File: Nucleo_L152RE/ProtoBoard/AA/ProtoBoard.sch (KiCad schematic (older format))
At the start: 114 parts, among them CON1 USB-MICRO-B, J1 EXT1, J2 EXT2, J3 EXTPower, P1 Power, P10 OW2_A, P11 GND1, P12 I2C1_B, P13 I2C2_B, P14 SW_1_6, P15 WS1, P16 WS2, P17 MS2, P18 WS3, P19 WS4, P2 VinPower, P20 GND2, P21 Hole, P22 MS3, P23 OW3_A, P24 OW4_A, P25 MS4, P26 Hole, P27 Hole, P28 RGB1, P29 Ant, P3 USART2, P30 Hole, P4 SWD Header, P5 USART1, P6 MS1, P7 I2C1_A, P8 I2C2_A, P9 OW1_A, Q1 SI2323DS, SW1 MomentarySwitch, U2 Nucleo-L152RE-CN7, U3 Nucleo-L152RE-CN10, U5 MT3329_GPS, U6 S25FL127S, U7 RFM69HW

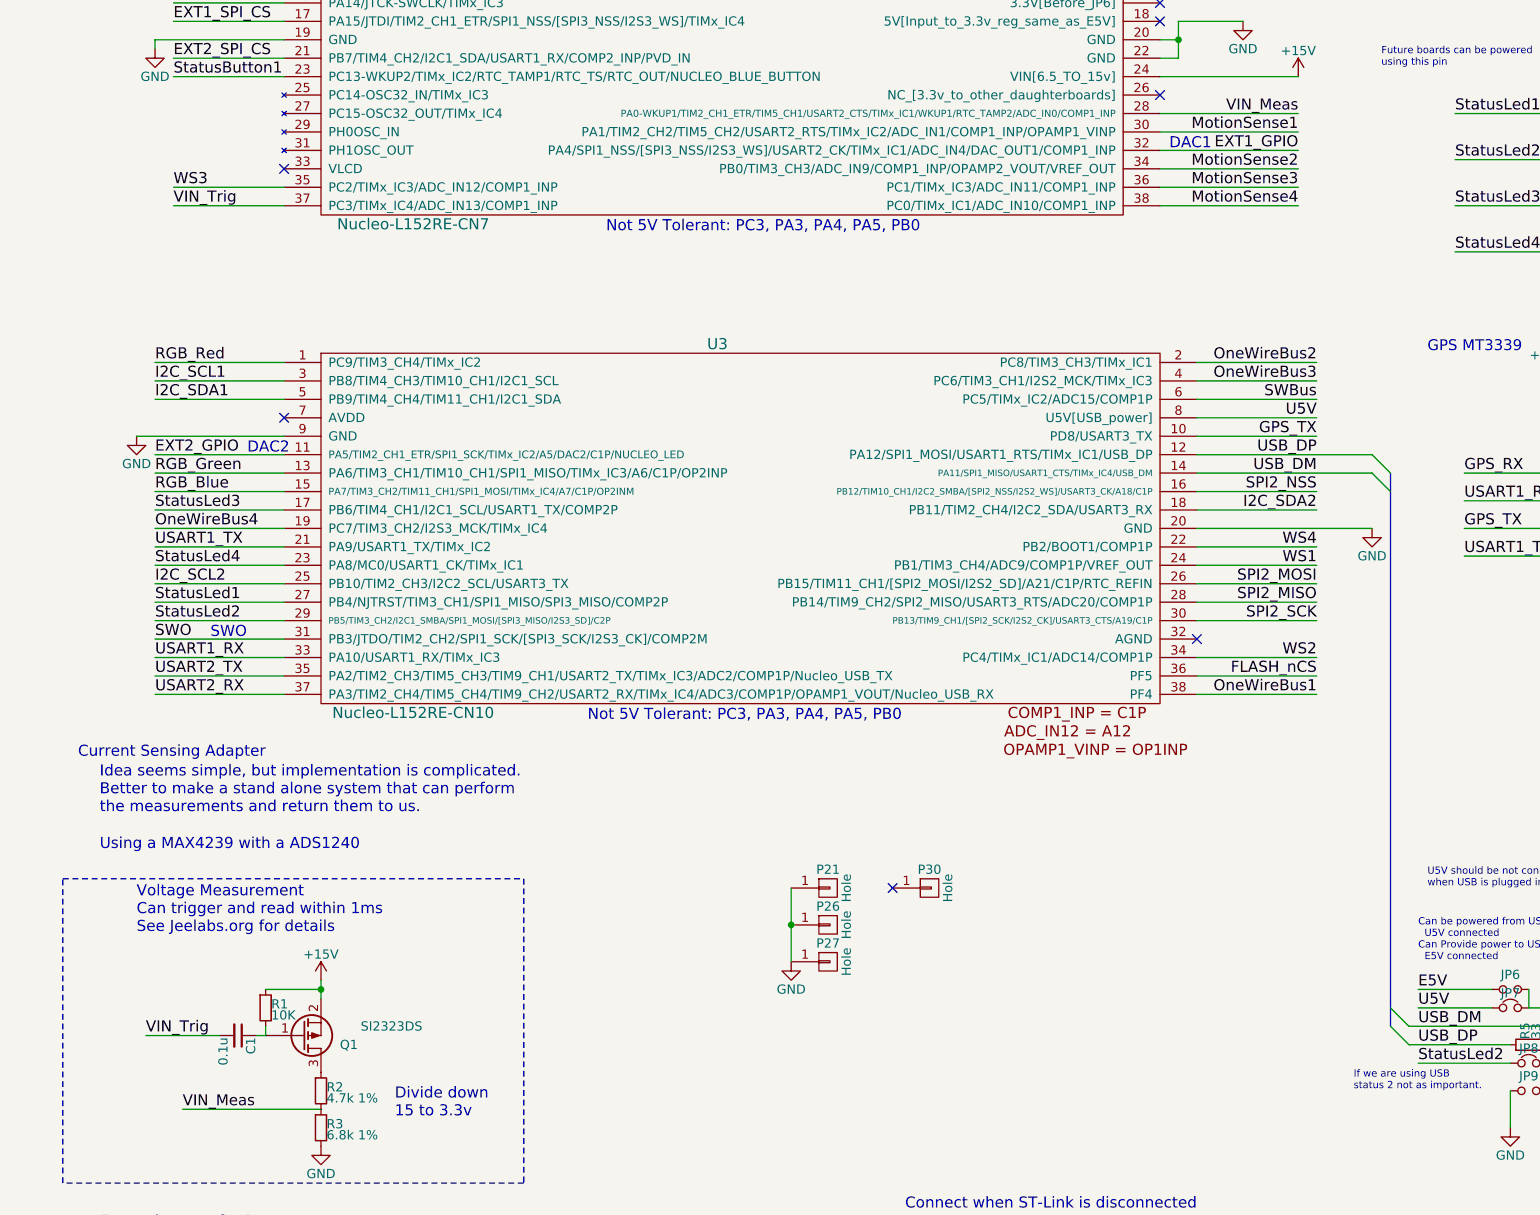
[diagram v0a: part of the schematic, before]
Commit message: Fixed Flash and Pmos footprints.  Added symbol part for schematic.
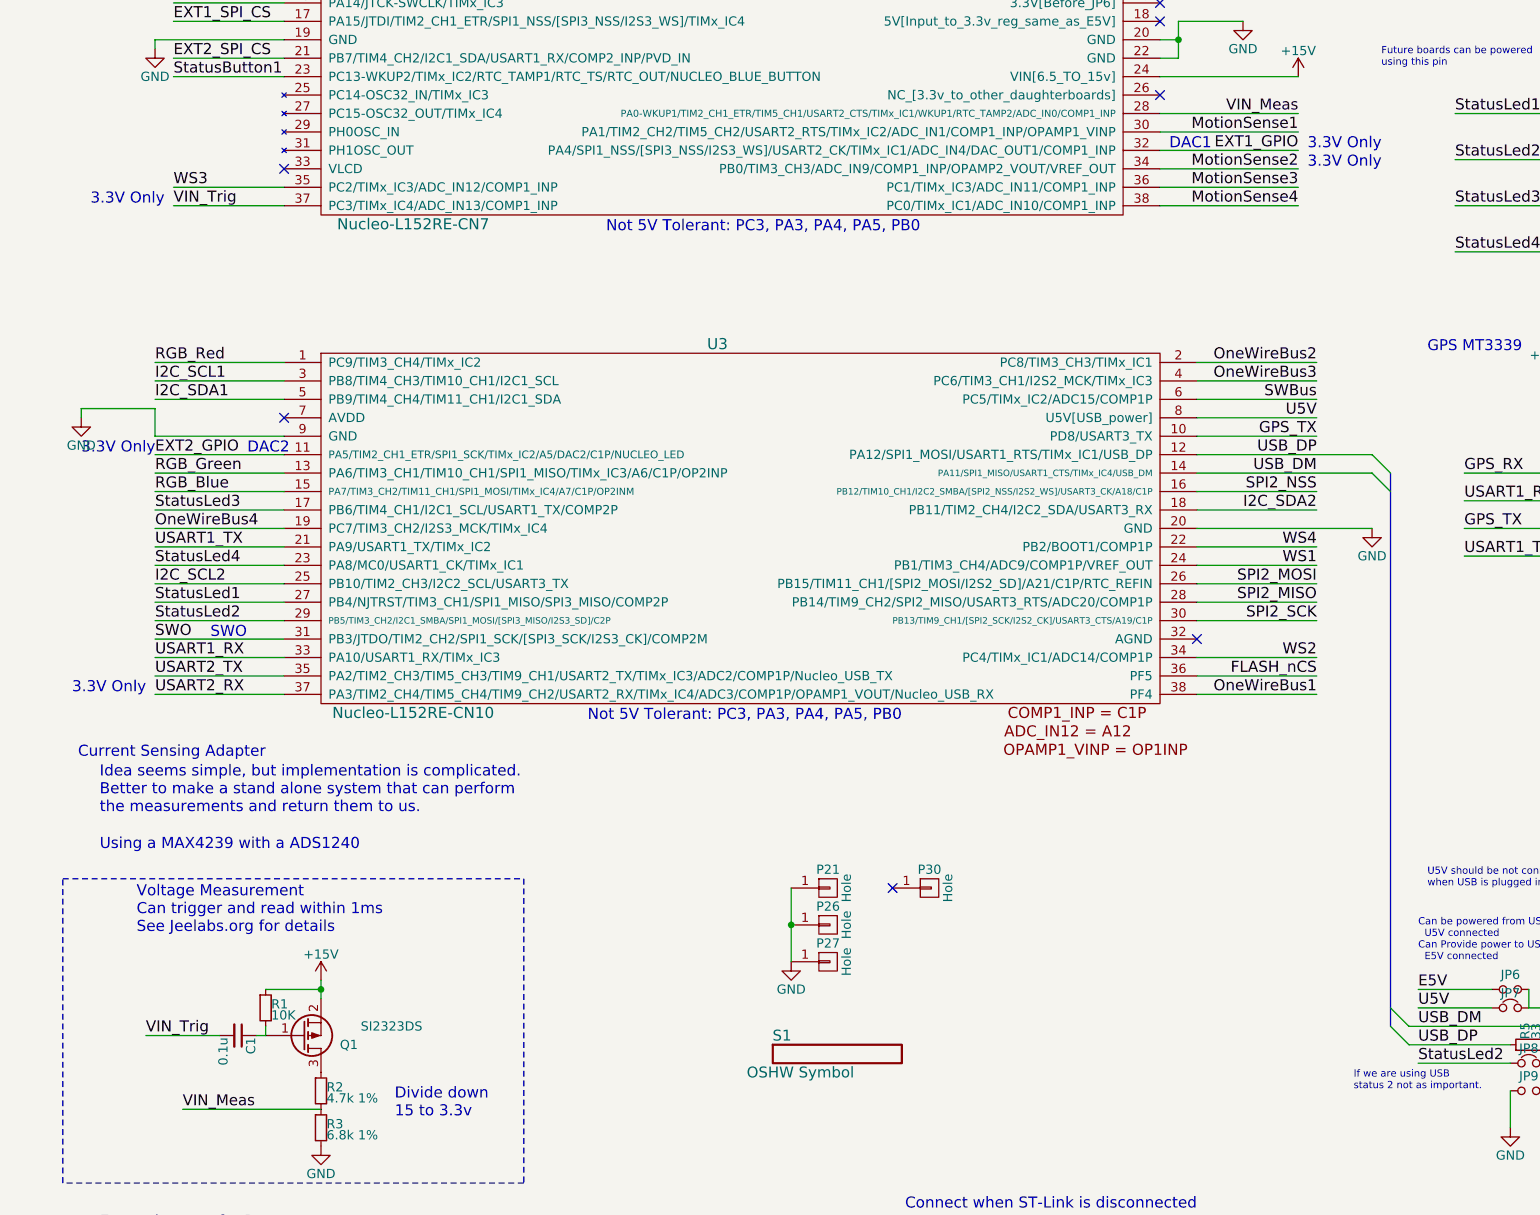
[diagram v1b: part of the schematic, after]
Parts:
- added S1: OSHW Symbol, Symbols:Symbol_OSHW-Logo_SilkScreen, symbol Symbol
- Q1: footprint SMD_Packages:SOT-323 -> nucleo:TO-236
- U6: footprint SMD_Packages:SOIC-8-N -> nucleo:SOIC-8-FLASH
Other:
- note added: "3.3V Only"
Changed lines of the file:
@@
 Sheet 1 1
 Title "Expansion Board For STM32 Nucleo-L152RE"
-Date "Wednesday, April 01, 2015"
+Date "Sunday, April 05, 2015"
 Rev "AA"
-Comp "NA"
-Comment1 ""
+Comp "Open Source Hardware"
+Comment1 "Creative Commons - Share Alike"
 Comment2 ""
 Comment3 ""
@@
 F 0 "U6" H 10250 1800 60  0000 C CNN
 F 1 "S25FL127S" H 10100 1300 60  0000 C CNN
-F 2 "SMD_Packages:SOIC-8-N" H 10250 1550 60  0001 C CNN
+F 2 "nucleo:SOIC-8-FLASH" H 10250 1550 60  0001 C CNN
 F 3 "" H 10250 1550 60  0000 C CNN
 	1    10250 1550
@@
 F 0 "Q1" H 2100 7550 50  0000 R CNN
 F 1 "SI2323DS" H 2450 7450 50  0000 R CNN
-F 2 "SMD_Packages:SOT-323" H 2000 7600 29  0001 C CNN
+F 2 "nucleo:TO-236" H 2000 7600 29  0001 C CNN
 F 3 "http://www.vishay.com/docs/72024/72024.pdf" H 1800 7500 60  0001 C CNN
 	1    1800 7500
@@
 F 1 "600 Ohm" V 9880 8610 50  0000 L CNN
 F 2 "Resistors_SMD:R_0603_HandSoldering" H 9850 8650 60  0001 C CNN
-F 3 "http://search.murata.co.jp/Ceramy/image/img/PDF/ENG/L0075S0103LQH3NP_G0.pdf" H 9850 8650 60  0001 C CNN
+F 3 "http://www.digikey.com/product-detail/en/MI0603J601R-10/240-2371-1-ND/806731" H 9850 8650 60  0001 C CNN
 	1    9850 8650
 	0    -1   -1   0
@@
 F 1 "600 Ohm" V 9900 7950 50  0000 L CNN
 F 2 "Resistors_SMD:R_0603_HandSoldering" H 9850 8350 60  0001 C CNN
-F 3 "http://search.murata.co.jp/Ceramy/image/img/PDF/ENG/L0075S0103LQH3NP_G0.pdf" H 9850 8350 60  0001 C CNN
+F 3 "http://www.digikey.com/product-detail/en/MI0603J601R-10/240-2371-1-ND/806731" H 9850 8350 60  0001 C CNN
 	1    9850 8350
 	0    -1   -1   0
@@
 L GND #PWR054
 U 1 1 5525ED88
-P 900 4250
-F 0 "#PWR054" H 900 4000 50  0001 C CNN
-F 1 "GND" H 900 4100 50  0000 C CNN
-F 2 "" H 900 4250 60  0000 C CNN
-F 3 "" H 900 4250 60  0000 C CNN
-	1    900  4250
+P 600 4150
+F 0 "#PWR054" H 600 3900 50  0001 C CNN
+F 1 "GND" H 600 4000 50  0000 C CNN
+F 2 "" H 600 4150 60  0000 C CNN
+F 3 "" H 600 4150 60  0000 C CNN
+	1    600  4150
 	1    0    0    -1
 $EndComp
@@
 	1000 2100 1000 2150
 Wire Wire Line
-	900  4250 1700 4250
-Wire Wire Line
 	6650 4750 7600 4750
 Wire Wire Line
@@
 Wire Wire Line
 	4450 6700 4450 7100
+Text Notes 7250 2800 0    60   ~ 0
+3.3V Only
+Text Notes 600  4350 0    60   ~ 0
+3.3V Only
+Wire Wire Line
+	1700 4250 1000 4250
+Wire Wire Line
+	1000 4250 1000 4100
+Wire Wire Line
+	1000 4100 600  4100
+Wire Wire Line
+	600  4100 600  4150
+Text Notes 550  5650 0    60   ~ 0
+3.3V Only
+Text Notes 7250 2700 0    60   ~ 0
+3.3V Only
+Text Notes 650  3000 0    60   ~ 0
+3.3V Only
+$Comp
+L Symbol S1
+U 1 1 552F8EA1
+P 4650 7600
+F 0 "S1" H 4400 7700 59  0000 C CNN
+F 1 "OSHW Symbol" H 4500 7500 59  0000 C CNN
+F 2 "Symbols:Symbol_OSHW-Logo_SilkScreen" H 4650 7600 59  0001 C CNN
+F 3 "" H 4650 7600 59  0000 C CNN
+	1    4650 7600
+	1    0    0    -1
+$EndComp
 $EndSCHEMATC

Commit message: Adding part details to schematic, creating BOM tools.
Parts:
- CON1: Digikey Part Number (none) -> 609-4053-1-ND; Digikey URL (none) -> http://www.digikey.com/product-detail/en/10104111-0001LF/60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
- D1: Digikey Part Number (none) -> 160-1447-1-ND; Digikey URL (none) -> http://www.digikey.com/product-detail/en/LTST-C191KRKT/160-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
- D2: Digikey Part Number (none) -> 160-1448-1-ND; Digikey URL (none) -> http://www.digikey.com/product-detail/en/LTST-C191KSKT/160-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
- D3: Digikey Part Number (none) -> 160-1446-1-ND; Digikey URL (none) -> http://www.digikey.com/product-detail/en/LTST-C191KGKT/160-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
- D4: Digikey Part Number (none) -> 160-1647-1-ND; Digikey URL (none) -> http://www.digikey.com/product-detail/en/LTST-C191TBKT/160-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
- J1, J2, J3: Digikey Part Number (none) -> RJLSE4238101TTR-ND; Digikey URL (none) -> http://www.digikey.com/product-detail/en/RJLSE4238101T/RJLS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
- L3, L4: Digikey Part Number (none) -> 240-2371-1-ND; Digikey URL (none) -> http://www.digikey.com/product-detail/en/MI0603J601R-10/240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
- SW1: Digikey Part Number (none) -> 450-1650-ND; Digikey URL (none) -> http://www.digikey.com/product-detail/en/1825910-6/450-1650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
- U6: Digikey Part Number (none) -> SI2323DS-T1-E3CT-ND; Digikey URL (none) -> http://www.digikey.com/product-detail/en/SI2323DS-T1-E3/SI2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
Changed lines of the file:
@@
 F 1 "S25FL127S" H 10100 1300 60  0000 C CNN
 F 2 "nucleo:SOIC-8-FLASH" H 10250 1550 60  0001 C CNN
-F 3 "" H 10250 1550 60  0000 C CNN
+F 3 "http://www.digikey.com/product-detail/en/SI2323DS-T1-E3/SI2323DS-T1-E3CT-ND" H 10250 1550 60  0001 C CNN
+F 4 "SI2323DS-T1-E3CT-ND" H 10250 1550 60  0001 C CNN "Digikey Part Number"
+F 5 "http://www.digikey.com/product-detail/en/SI2323DS-T1-E3/SI2323DS-T1-E3CT-ND" H 10250 1550 60  0001 C CNN "Digikey URL"
 	1    10250 1550
 	1    0    0    -1
@@
 F 2 "nucleo:RJ45_SMD" H 9100 9650 60  0001 C CNN
 F 3 "http://www.digikey.com/product-detail/en/RJLSE4238101T/RJLSE4238101TTR-ND/1979556" H 9100 9650 60  0001 C CNN
+F 4 "RJLSE4238101TTR-ND" H 9100 9650 60  0001 C CNN "Digikey Part Number"
+F 5 "http://www.digikey.com/product-detail/en/RJLSE4238101T/RJLSE4238101TTR-ND/1979556" H 9100 9650 60  0001 C CNN "Digikey URL"
 	1    9100 9650
 	0    1    1    0
@@
 F 2 "nucleo:RJ45_SMD" H 11150 9650 60  0001 C CNN
 F 3 "http://www.digikey.com/product-detail/en/RJLSE4238101T/RJLSE4238101TTR-ND/1979556" H 11150 9650 60  0001 C CNN
+F 4 "RJLSE4238101TTR-ND" H 11150 9650 60  0001 C CNN "Digikey Part Number"
+F 5 "http://www.digikey.com/product-detail/en/RJLSE4238101T/RJLSE4238101TTR-ND/1979556" H 11150 9650 60  0001 C CNN "Digikey URL"
 	1    11150 9650
 	0    1    1    0
@@
 F 2 "Resistors_SMD:R_0603_HandSoldering" H 9850 8650 60  0001 C CNN
 F 3 "http://www.digikey.com/product-detail/en/MI0603J601R-10/240-2371-1-ND/806731" H 9850 8650 60  0001 C CNN
+F 4 "240-2371-1-ND" V 9850 8650 60  0001 C CNN "Digikey Part Number"
+F 5 "http://www.digikey.com/product-detail/en/MI0603J601R-10/240-2371-1-ND/" V 9850 8650 60  0001 C CNN "Digikey URL"
 	1    9850 8650
 	0    -1   -1   0
@@
 F 2 "Resistors_SMD:R_0603_HandSoldering" H 9850 8350 60  0001 C CNN
 F 3 "http://www.digikey.com/product-detail/en/MI0603J601R-10/240-2371-1-ND/806731" H 9850 8350 60  0001 C CNN
+F 4 "240-2371-1-ND" V 9850 8350 60  0001 C CNN "Digikey Part Number"
+F 5 "http://www.digikey.com/product-detail/en/MI0603J601R-10/240-2371-1-ND/" V 9850 8350 60  0001 C CNN "Digikey URL"
 	1    9850 8350
 	0    -1   -1   0
@@
 F 1 "Red" H 8800 2420 50  0000 L CNN
 F 2 "nucleo:LED_0603" V 8950 2500 60  0001 C CNN
-F 3 "" V 8950 2500 60  0000 C CNN
+F 3 "http://optoelectronics.liteon.com/upload/download/DS22-2000-223/S_110_LTST-C191KRKT.pdf" V 8950 2500 60  0001 C CNN
+F 4 "160-1447-1-ND" H 8950 2500 60  0001 C CNN "Digikey Part Number"
+F 5 "http://www.digikey.com/product-detail/en/LTST-C191KRKT/160-1447-1-ND/386836" H 8950 2500 60  0001 C CNN "Digikey URL"
 	1    8950 2500
 	1    0    0    -1
@@
 F 1 "Yellow" H 8800 2670 50  0000 L CNN
 F 2 "nucleo:LED_0603" V 8950 2750 60  0001 C CNN
-F 3 "" V 8950 2750 60  0000 C CNN
+F 3 "http://optoelectronics.liteon.com/upload/download/DS22-2000-224/S_110_LTST-C191KSKT.pdf" V 8950 2750 60  0001 C CNN
+F 4 "160-1448-1-ND" H 8950 2750 60  0001 C CNN "Digikey Part Number"
+F 5 "http://www.digikey.com/product-detail/en/LTST-C191KSKT/160-1448-1-ND" H 8950 2750 60  0001 C CNN "Digikey URL"
 	1    8950 2750
 	1    0    0    -1
@@
 F 2 "nucleo:Tact_switch" H 10250 2400 60  0001 C CNN
 F 3 "" H 10250 2400 60  0000 C CNN
+F 4 "450-1650-ND" H 10250 2400 60  0001 C CNN "Digikey Part Number"
+F 5 "http://www.digikey.com/product-detail/en/1825910-6/450-1650-ND" H 10250 2400 60  0001 C CNN "Digikey URL"
 	1    10250 2400
 	1    0    0    -1
@@
 F 2 "nucleo:USB_micro_AB" H 9350 7450 50  0001 C CNN
 F 3 "http://www.digikey.com/product-detail/en/10104111-0001LF/609-4053-1-ND/2350359" H 9350 7450 50  0001 C CNN
+F 4 "609-4053-1-ND" H 9350 7550 60  0001 C CNN "Digikey Part Number"
+F 5 "http://www.digikey.com/product-detail/en/10104111-0001LF/609-4053-1-ND" H 9350 7550 60  0001 C CNN "Digikey URL"
 	1    9350 7550
 	1    0    0    -1
@@
 F 1 "Green" H 8800 2920 50  0000 L CNN
 F 2 "nucleo:LED_0603" V 8950 3000 60  0001 C CNN
-F 3 "" V 8950 3000 60  0000 C CNN
+F 3 "http://optoelectronics.liteon.com/upload/download/DS22-2000-228/S_110_LTST-C191KGKT.pdf" V 8950 3000 60  0001 C CNN
+F 4 "160-1446-1-ND" H 8950 3000 60  0001 C CNN "Digikey Part Number"
+F 5 "http://www.digikey.com/product-detail/en/LTST-C191KGKT/160-1446-1-ND" H 8950 3000 60  0001 C CNN "Digikey URL"
 	1    8950 3000
 	1    0    0    -1
@@
 F 1 "Blue" H 8800 3170 50  0000 L CNN
 F 2 "nucleo:LED_0603" V 8950 3250 60  0001 C CNN
-F 3 "" V 8950 3250 60  0000 C CNN
+F 3 "http://optoelectronics.liteon.com/upload/download/DS22-2000-230/S_110_LTST-C191TBKT.pdf" V 8950 3250 60  0001 C CNN
+F 4 "160-1647-1-ND" H 8950 3250 60  0001 C CNN "Digikey Part Number"
+F 5 "http://www.digikey.com/product-detail/en/LTST-C191TBKT/160-1647-1-ND" H 8950 3250 60  0001 C CNN "Digikey URL"
 	1    8950 3250
 	1    0    0    -1
@@
 F 2 "nucleo:RJ45_SMD" H 2200 9100 60  0001 C CNN
 F 3 "http://www.digikey.com/product-detail/en/RJLSE4238101T/RJLSE4238101TTR-ND/1979556" H 2200 9100 60  0001 C CNN
+F 4 "RJLSE4238101TTR-ND" H 2200 9100 60  0001 C CNN "Digikey Part Number"
+F 5 "http://www.digikey.com/product-detail/en/RJLSE4238101T/RJLSE4238101TTR-ND/1979556" H 2200 9100 60  0001 C CNN "Digikey URL"
 	1    2200 9100
 	0    1    1    0
